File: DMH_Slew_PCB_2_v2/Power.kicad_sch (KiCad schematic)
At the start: 29 parts, among them J0 Conn_01x01, J101 IDC_02x08, J200 IDC_02x05, J50 Conn_01x08_PinHeader, J51 Conn_01x08_PinHeader, J60 Conn_01x08_PinHeader, J61 Conn_01x08_PinHeader, U1 TL074, U10 LM4040LP-10, U11 LM4040LP-10, U2 TL074, U3 TL074, U4 TL074

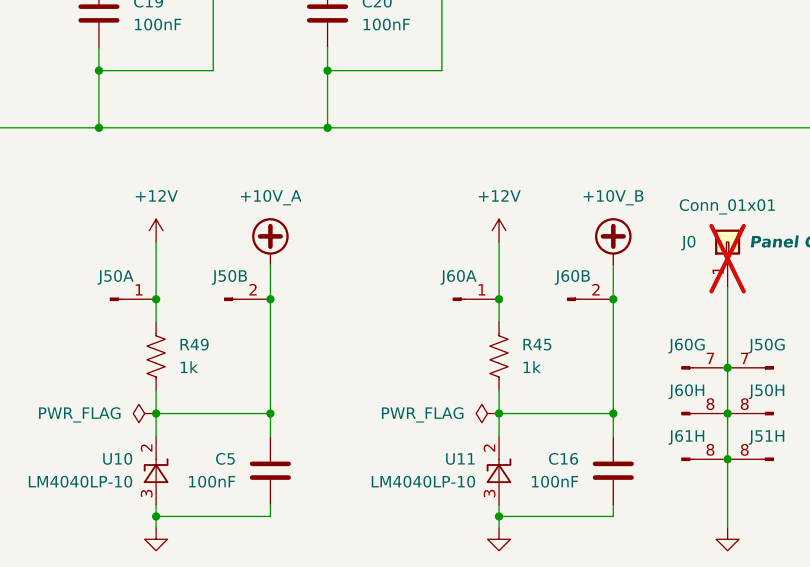
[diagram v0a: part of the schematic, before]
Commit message: PCB 2 component placement done
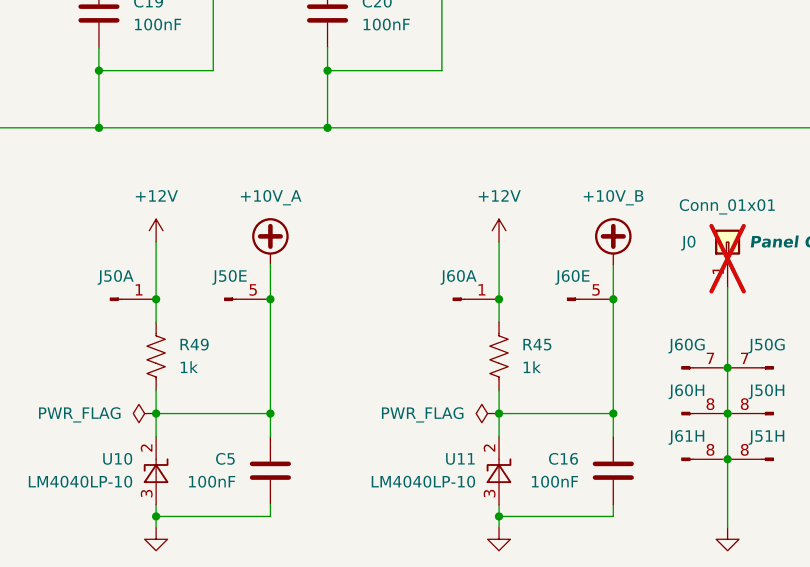
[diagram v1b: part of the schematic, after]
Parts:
- J50, J51, J60, J61: footprint Connector_PinHeader_2.54mm:PinHeader_1x08_P2.54mm_Vertical -> Connector_PinSocket_2.54mm:PinSocket_1x08_P2.54mm_Vertical
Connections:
- net +10V_A: now also J50.5 (Pin_5); no longer J50.2 (Pin_2)
- net +10V_B: now also J60.5 (Pin_5); no longer J60.2 (Pin_2)
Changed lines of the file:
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@@
 		(lib_id "SynthStuff:Conn_01x08_PinHeader")
 		(at 140.97 165.1 0)
-		(unit 2)
+		(unit 5)
 		(exclude_from_sim no)
 		(in_bom yes)
@@
 			)
 		)
-		(property "Footprint" "Connector_PinHeader_2.54mm:PinHeader_1x08_P2.54mm_Vertical"
+		(property "Footprint" "Connector_PinSocket_2.54mm:PinSocket_1x08_P2.54mm_Vertical"
 			(at 140.97 165.1 0)
 			(effects
@@
 				(path "/58f4306d-5387-4983-bb08-41a2313fd315/0cdf34b2-39cd-4d9e-981a-97cd34791509"
 					(reference "J60")
-					(unit 2)
+					(unit 5)
 				)
 			)
@@
 			)
 		)
-		(property "Footprint" "Connector_PinHeader_2.54mm:PinHeader_1x08_P2.54mm_Vertical"
+		(property "Footprint" "Connector_PinSocket_2.54mm:PinSocket_1x08_P2.54mm_Vertical"
 			(at 128.27 165.1 0)
 			(effects
@@
 			)
 		)
-		(property "Footprint" "Connector_PinHeader_2.54mm:PinHeader_1x08_P2.54mm_Vertical"
+		(property "Footprint" "Connector_PinSocket_2.54mm:PinSocket_1x08_P2.54mm_Vertical"
 			(at 163.83 182.88 0)
 			(effects
@@
 			)
 		)
-		(property "Footprint" "Connector_PinHeader_2.54mm:PinHeader_1x08_P2.54mm_Vertical"
+		(property "Footprint" "Connector_PinSocket_2.54mm:PinSocket_1x08_P2.54mm_Vertical"
 			(at 153.67 177.8 0)
 			(effects
@@
 		(lib_id "SynthStuff:Conn_01x08_PinHeader")
 		(at 102.87 165.1 0)
-		(unit 2)
+		(unit 5)
 		(exclude_from_sim no)
 		(in_bom yes)
@@
 			)
 		)
-		(property "Footprint" "Connector_PinHeader_2.54mm:PinHeader_1x08_P2.54mm_Vertical"
+		(property "Footprint" "Connector_PinSocket_2.54mm:PinSocket_1x08_P2.54mm_Vertical"
 			(at 102.87 165.1 0)
 			(effects
@@
 				(path "/58f4306d-5387-4983-bb08-41a2313fd315/0cdf34b2-39cd-4d9e-981a-97cd34791509"
 					(reference "J50")
-					(unit 2)
+					(unit 5)
 				)
 			)
@@
 			)
 		)
-		(property "Footprint" "Connector_PinHeader_2.54mm:PinHeader_1x08_P2.54mm_Vertical"
+		(property "Footprint" "Connector_PinSocket_2.54mm:PinSocket_1x08_P2.54mm_Vertical"
 			(at 163.83 172.72 0)
 			(effects
@@
 			)
 		)
-		(property "Footprint" "Connector_PinHeader_2.54mm:PinHeader_1x08_P2.54mm_Vertical"
+		(property "Footprint" "Connector_PinSocket_2.54mm:PinSocket_1x08_P2.54mm_Vertical"
 			(at 90.17 165.1 0)
 			(effects
@@
 			)
 		)
-		(property "Footprint" "Connector_PinHeader_2.54mm:PinHeader_1x08_P2.54mm_Vertical"
+		(property "Footprint" "Connector_PinSocket_2.54mm:PinSocket_1x08_P2.54mm_Vertical"
 			(at 153.67 172.72 0)
 			(effects
@@
 			)
 		)
-		(property "Footprint" "Connector_PinHeader_2.54mm:PinHeader_1x08_P2.54mm_Vertical"
+		(property "Footprint" "Connector_PinSocket_2.54mm:PinSocket_1x08_P2.54mm_Vertical"
 			(at 163.83 177.8 0)
 			(effects
@@
 			)
 		)
-		(property "Footprint" "Connector_PinHeader_2.54mm:PinHeader_1x08_P2.54mm_Vertical"
+		(property "Footprint" "Connector_PinSocket_2.54mm:PinSocket_1x08_P2.54mm_Vertical"
 			(at 153.67 182.88 0)
 			(effects

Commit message: PCB 1 component placement ongoing
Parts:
- J0: Function Panel GND -> GND
- renumbered J101 to J100
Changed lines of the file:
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@@
 			)
 		)
-		(property "Function" "Panel GND"
-			(at 166.37 158.75 90)
+		(property "Function" "GND"
+			(at 162.814 158.496 90)
 			(effects
 				(font
@@
 		(dnp no)
 		(fields_autoplaced yes)
-		(property "Reference" "J101"
+		(property "Reference" "J100"
 			(at 25.4 168.91 0)
 			(effects
@@
 			(project "DMH-Kosmo-10cm-PCB"
 				(path "/58f4306d-5387-4983-bb08-41a2313fd315/0cdf34b2-39cd-4d9e-981a-97cd34791509"
-					(reference "J101")
+					(reference "J100")
 					(unit 1)
 				)

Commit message: Updated Log circuit
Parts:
- renumbered J60 to J50, J61 to J51, J50 to J60, J51 to J61
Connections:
- net +12V: no longer J50.1 (Pin_1), J60.1 (Pin_1)
- net GND: now also J50.1 (Pin_1), J60.1 (Pin_1)
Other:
- moved on the sheet: J50G, J50H, J51H, J60G, J60H, J61H
